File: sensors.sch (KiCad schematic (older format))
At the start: 0 parts

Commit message: Schematic: EEPROM + IMU
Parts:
- added C?: 10n, symbol C_Small
- added C? (x2): 100n, symbol C_Small
- added U?: MPU-9250, symbol MPU-9250
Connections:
- new net: C?.1, U?.10 (REGOUT)
- new net +3.3V_A: C?.1, C?.1, U?.13 (VDD), U?.19 (RESV), U?.8 (VDDIO)
- new net GND: C?.2, C?.2, C?.2, U?.18 (GND), U?.20 (RESV)
- new net SPI1_CS: U?.22 (nCS)
- new net SPI1_INT: U?.12 (INT)
- new net SPI1_MISO: U?.9 (AD0/SD0)
- new net SPI1_MOSI: U?.24 (SDA/SDI)
- new net SPI1_SCK: U?.23 (SCL/SCLK)
- no-connect marks 0 -> 13
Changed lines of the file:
@@
 LIBS:IRF
 LIBS:Comp2014
+LIBS:robocape-cache
 EELAYER 25 0
 EELAYER END
 $Descr A4 11693 8268
 encoding utf-8
-Sheet 1 3
+Sheet 2 4
 Title ""
 Date ""
@@
 Comment4 ""
 $EndDescr
+$Comp
+L MPU-9250 U?
+U 1 1 55A53A6C
+P 3750 2800
+F 0 "U?" H 4150 3600 60  0000 C CNN
+F 1 "MPU-9250" H 3500 3600 60  0000 C CNN
+F 2 "" H 3750 3400 60  0000 C CNN
+F 3 "" H 3750 3400 60  0000 C CNN
+	1    3750 2800
+	1    0    0    -1
+$EndComp
+NoConn ~ 2950 3500
+NoConn ~ 2950 3400
+NoConn ~ 2950 3300
+NoConn ~ 2950 3200
+NoConn ~ 2950 3100
+NoConn ~ 2950 3000
+NoConn ~ 2950 2900
+NoConn ~ 2950 2800
+NoConn ~ 2950 2700
+$Comp
+L +3.3V_A #PWR?
+U 1 1 55A53AEE
+P 2450 2125
+F 0 "#PWR?" H 2450 2085 30  0001 C CNN
+F 1 "+3.3V_A" H 2450 2235 30  0000 C CNN
+F 2 "" H 2450 2125 60  0000 C CNN
+F 3 "" H 2450 2125 60  0000 C CNN
+	1    2450 2125
+	1    0    0    -1
+$EndComp
+Wire Wire Line
+	2450 2150 2950 2150
+Wire Wire Line
+	2900 2150 2900 2250
+Wire Wire Line
+	2900 2250 2950 2250
+Connection ~ 2900 2150
+$Comp
+L GND #PWR?
+U 1 1 55A53B15
+P 2450 2475
+F 0 "#PWR?" H 2450 2225 50  0001 C CNN
+F 1 "GND" H 2450 2325 50  0000 C CNN
+F 2 "" H 2450 2475 60  0000 C CNN
+F 3 "" H 2450 2475 60  0000 C CNN
+	1    2450 2475
+	1    0    0    -1
+$EndComp
+Wire Wire Line
+	2450 2450 2950 2450
+$Comp
+L C_Small C?
+U 1 1 55A53B36
+P 2725 2300
+F 0 "C?" H 2735 2370 50  0000 L CNN
+F 1 "10n" H 2735 2220 50  0000 L CNN
+F 2 "" H 2725 2300 60  0000 C CNN
+F 3 "" H 2725 2300 60  0000 C CNN
+	1    2725 2300
+	1    0    0    -1
+$EndComp
+$Comp
+L C_Small C?
+U 1 1 55A53B7A
+P 2450 2300
+F 0 "C?" H 2460 2370 50  0000 L CNN
+F 1 "100n" H 2460 2220 50  0000 L CNN
+F 2 "" H 2450 2300 60  0000 C CNN
+F 3 "" H 2450 2300 60  0000 C CNN
+	1    2450 2300
+	1    0    0    -1
+$EndComp
+Wire Wire Line
+	2450 2125 2450 2200
+Connection ~ 2450 2150
+Wire Wire Line
+	2450 2400 2450 2475
+Connection ~ 2450 2450
+Wire Wire Line
+	2725 2400 2725 2450
+Connection ~ 2725 2450
+Wire Wire Line
+	2725 2200 2725 2150
+Connection ~ 2725 2150
+NoConn ~ 4550 2150
+NoConn ~ 4550 2250
+Text HLabel 4600 2400 2    39   Input ~ 0
+SPI1_SCK
+Wire Wire Line
+	4600 2400 4550 2400
+Text HLabel 4600 2500 2    39   Input ~ 0
+SPI1_MOSI
+Text HLabel 4600 2650 2    39   Input ~ 0
+SPI1_MISO
+Text HLabel 4600 2800 2    39   Input ~ 0
+SPI1_CS
+Wire Wire Line
+	4600 2500 4550 2500
+Wire Wire Line
+	4600 2650 4550 2650
+Wire Wire Line
+	4550 2800 4600 2800
+Text HLabel 4600 2950 2    39   Input ~ 0
+SPI1_INT
+Wire Wire Line
+	4600 2950 4550 2950
+$Comp
+L C_Small C?
+U 1 1 55A53E9E
+P 5025 3150
+F 0 "C?" H 5035 3220 50  0000 L CNN
+F 1 "100n" H 5035 3070 50  0000 L CNN
+F 2 "" H 5025 3150 60  0000 C CNN
+F 3 "" H 5025 3150 60  0000 C CNN
+	1    5025 3150
+	1    0    0    -1
+$EndComp
+NoConn ~ 4550 3150
+NoConn ~ 4550 3300
+$Comp
+L +3.3V_A #PWR?
+U 1 1 55A53F56
+P 4725 3400
+F 0 "#PWR?" H 4725 3360 30  0001 C CNN
+F 1 "+3.3V_A" H 4725 3510 30  0000 C CNN
+F 2 "" H 4725 3400 60  0000 C CNN
+F 3 "" H 4725 3400 60  0000 C CNN
+	1    4725 3400
+	1    0    0    -1
+$EndComp
+Wire Wire Line
+	4725 3400 4550 3400
+$Comp
+L GND #PWR?
+U 1 1 55A53F96
+P 4725 3500
+F 0 "#PWR?" H 4725 3250 50  0001 C CNN
+F 1 "GND" H 4725 3350 50  0000 C CNN
+F 2 "" H 4725 3500 60  0000 C CNN
+F 3 "" H 4725 3500 60  0000 C CNN
+	1    4725 3500
+	1    0    0    -1
+$EndComp
+Wire Wire Line
+	4725 3500 4550 3500
+$Comp
+L GND #PWR?
+U 1 1 55A53FE1
+P 5025 3300
+F 0 "#PWR?" H 5025 3050 50  0001 C CNN
+F 1 "GND" H 5025 3150 50  0000 C CNN
+F 2 "" H 5025 3300 60  0000 C CNN
+F 3 "" H 5025 3300 60  0000 C CNN
+	1    5025 3300
+	1    0    0    -1
+$EndComp
+Wire Wire Line
+	4550 3050 5025 3050
+Wire Wire Line
+	5025 3250 5025 3300
 $EndSCHEMATC

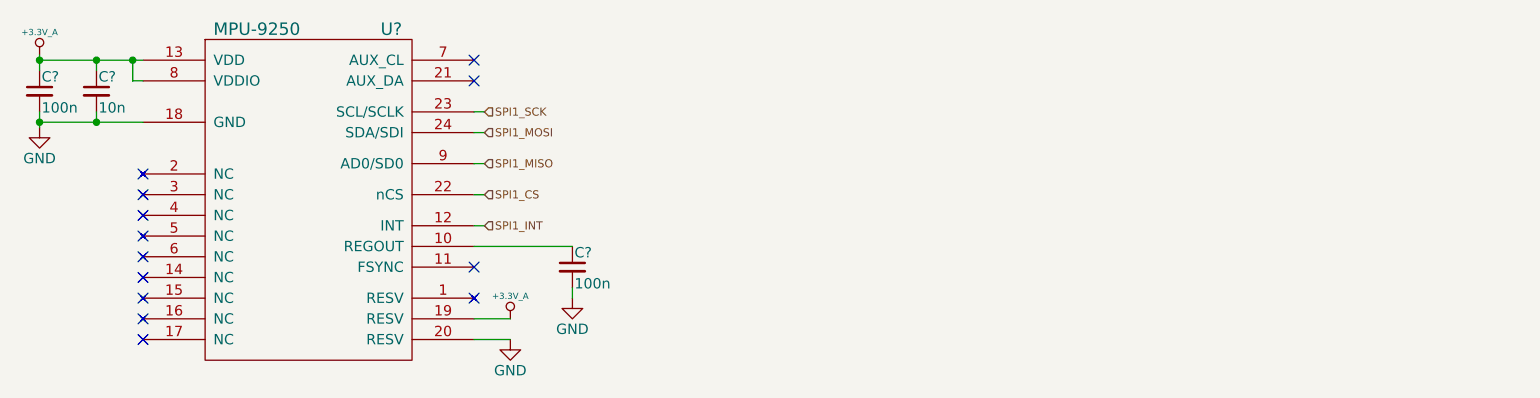
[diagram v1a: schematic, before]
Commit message: Schematic: Barometer
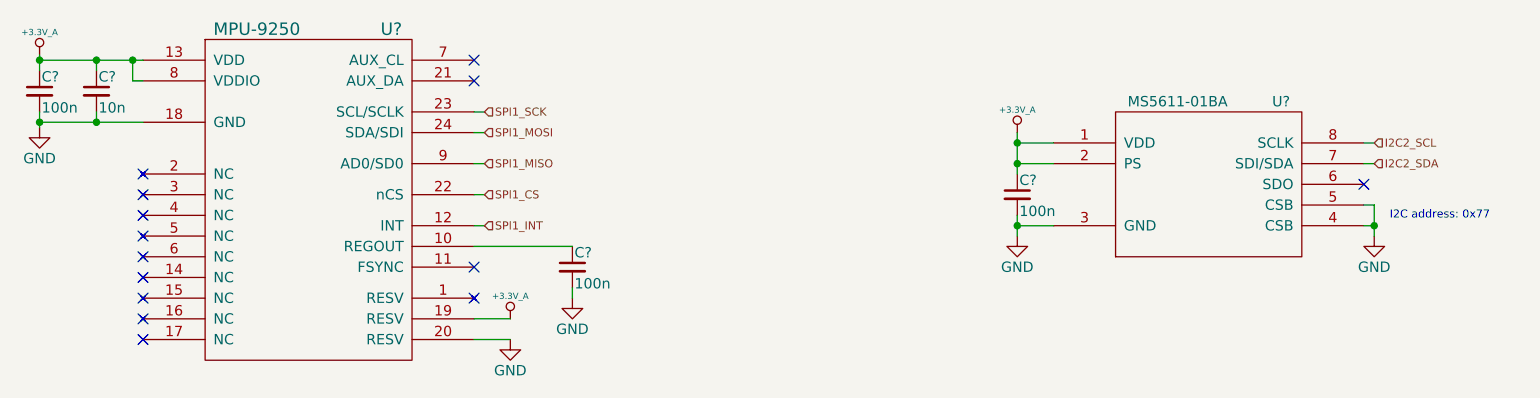
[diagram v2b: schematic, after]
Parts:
- added C?: 100n, symbol C_Small
- added U?: MS5611-01BA, MODULE, symbol MS5611-01BA
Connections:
- net +3.3V_A: now also C?.1, U?.1 (VDD), U?.2 (PS)
- net GND: now also C?.2, U?.3 (GND), U?.4 (CSB), U?.5 (CSB)
- new net I2C2_SCL: U?.8 (SCLK)
- new net I2C2_SDA: U?.7 (SDI/SDA)
- no-connect marks 13 -> 14
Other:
- note added: "I2C address: 0x77\n"
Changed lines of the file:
@@
 $Descr A4 11693 8268
 encoding utf-8
-Sheet 2 4
+Sheet 4 4
 Title ""
 Date ""
@@
 $EndComp
 Wire Wire Line
-	2450 2150 2950 2150
+	2450 2150 2725 2150
+Wire Wire Line
+	2725 2150 2900 2150
+Wire Wire Line
+	2900 2150 2950 2150
 Wire Wire Line
 	2900 2150 2900 2250
@@
 $EndComp
 Wire Wire Line
-	2450 2450 2950 2450
+	2450 2450 2725 2450
+Wire Wire Line
+	2725 2450 2950 2450
 $Comp
 L C_Small C?
@@
 $EndComp
 Wire Wire Line
-	2450 2125 2450 2200
+	2450 2125 2450 2150
+Wire Wire Line
+	2450 2150 2450 2200
 Connection ~ 2450 2150
 Wire Wire Line
-	2450 2400 2450 2475
+	2450 2400 2450 2450
+Wire Wire Line
+	2450 2450 2450 2475
 Connection ~ 2450 2450
 Wire Wire Line
@@
 Wire Wire Line
 	5025 3250 5025 3300
+$Comp
+L MS5611-01BA U?
+U 1 1 55A562A6
+P 8100 2750
+F 0 "U?" H 8450 3150 50  0000 C CNN
+F 1 "MS5611-01BA" H 7950 3150 50  0000 C CNN
+F 2 "MODULE" H 8100 2750 50  0001 C CNN
+F 3 "DOCUMENTATION" H 8100 2750 50  0001 C CNN
+	1    8100 2750
+	1    0    0    -1
+$EndComp
+NoConn ~ 8850 2750
+$Comp
+L GND #PWR?
+U 1 1 55A56310
+P 8900 3000
+F 0 "#PWR?" H 8900 2750 50  0001 C CNN
+F 1 "GND" H 8900 2850 50  0000 C CNN
+F 2 "" H 8900 3000 60  0000 C CNN
+F 3 "" H 8900 3000 60  0000 C CNN
+	1    8900 3000
+	1    0    0    -1
+$EndComp
+Wire Wire Line
+	8850 2850 8900 2850
+Wire Wire Line
+	8900 2850 8900 2950
+Wire Wire Line
+	8900 2950 8900 3000
+Wire Wire Line
+	8850 2950 8900 2950
+Connection ~ 8900 2950
+Text HLabel 8900 2650 2    39   Input ~ 0
+I2C2_SDA
+Text HLabel 8900 2550 2    39   Input ~ 0
+I2C2_SCL
+Wire Wire Line
+	8900 2550 8850 2550
+Wire Wire Line
+	8850 2650 8900 2650
+$Comp
+L +3.3V_A #PWR?
+U 1 1 55A56473
+P 7175 2500
+F 0 "#PWR?" H 7175 2460 30  0001 C CNN
+F 1 "+3.3V_A" H 7175 2610 30  0000 C CNN
+F 2 "" H 7175 2500 60  0000 C CNN
+F 3 "" H 7175 2500 60  0000 C CNN
+	1    7175 2500
+	1    0    0    -1
+$EndComp
+$Comp
+L C_Small C?
+U 1 1 55A564A3
+P 7175 2800
+F 0 "C?" H 7185 2870 50  0000 L CNN
+F 1 "100n" H 7185 2720 50  0000 L CNN
+F 2 "" H 7175 2800 60  0000 C CNN
+F 3 "" H 7175 2800 60  0000 C CNN
+	1    7175 2800
+	1    0    0    -1
+$EndComp
+Wire Wire Line
+	7350 2650 7175 2650
+Wire Wire Line
+	7175 2500 7175 2550
+Wire Wire Line
+	7175 2550 7175 2650
+Wire Wire Line
+	7175 2650 7175 2700
+Wire Wire Line
+	7175 2900 7175 2950
+Wire Wire Line
+	7175 2950 7175 3000
+Wire Wire Line
+	7175 2950 7350 2950
+Connection ~ 7175 2650
+Wire Wire Line
+	7350 2550 7175 2550
+Connection ~ 7175 2550
+$Comp
+L GND #PWR?
+U 1 1 55A566F0
+P 7175 3000
+F 0 "#PWR?" H 7175 2750 50  0001 C CNN
+F 1 "GND" H 7175 2850 50  0000 C CNN
+F 2 "" H 7175 3000 60  0000 C CNN
+F 3 "" H 7175 3000 60  0000 C CNN
+	1    7175 3000
+	1    0    0    -1
+$EndComp
+Connection ~ 7175 2950
+Text Notes 8975 2925 0    39   ~ 0
+I2C address: 0x77\n
 $EndSCHEMATC

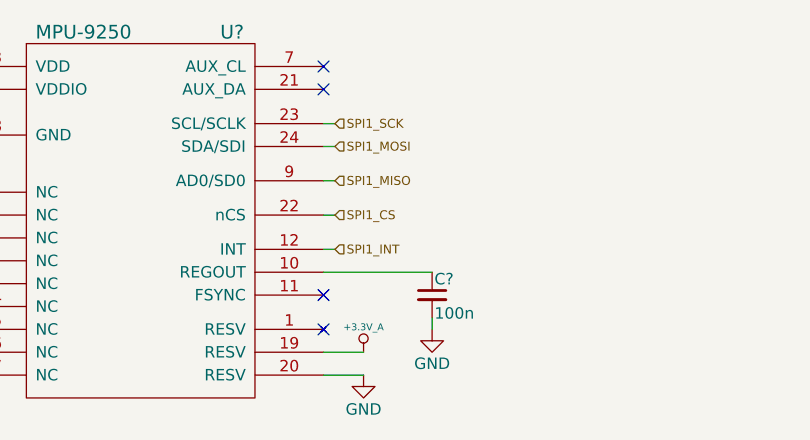
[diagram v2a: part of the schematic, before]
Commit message: Schematic: Xbee header
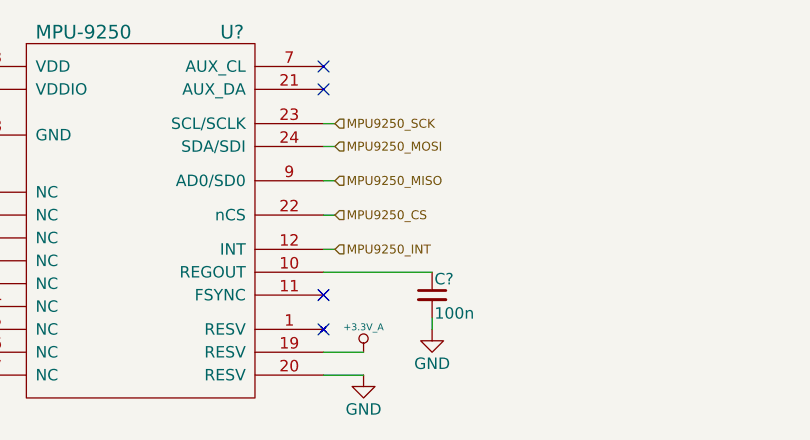
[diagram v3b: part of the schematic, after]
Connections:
- net SPI1_CS renamed MPU9250_CS
- net SPI1_INT renamed MPU9250_INT
- net SPI1_MISO renamed MPU9250_MISO
- net SPI1_MOSI renamed MPU9250_MOSI
- net SPI1_SCK renamed MPU9250_SCK
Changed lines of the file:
@@
 NoConn ~ 4550 2250
 Text HLabel 4600 2400 2    39   Input ~ 0
-SPI1_SCK
+MPU9250_SCK
 Wire Wire Line
 	4600 2400 4550 2400
 Text HLabel 4600 2500 2    39   Input ~ 0
-SPI1_MOSI
+MPU9250_MOSI
 Text HLabel 4600 2650 2    39   Input ~ 0
-SPI1_MISO
+MPU9250_MISO
 Text HLabel 4600 2800 2    39   Input ~ 0
-SPI1_CS
+MPU9250_CS
 Wire Wire Line
 	4600 2500 4550 2500
@@
 	4550 2800 4600 2800
 Text HLabel 4600 2950 2    39   Input ~ 0
-SPI1_INT
+MPU9250_INT
 Wire Wire Line
 	4600 2950 4550 2950

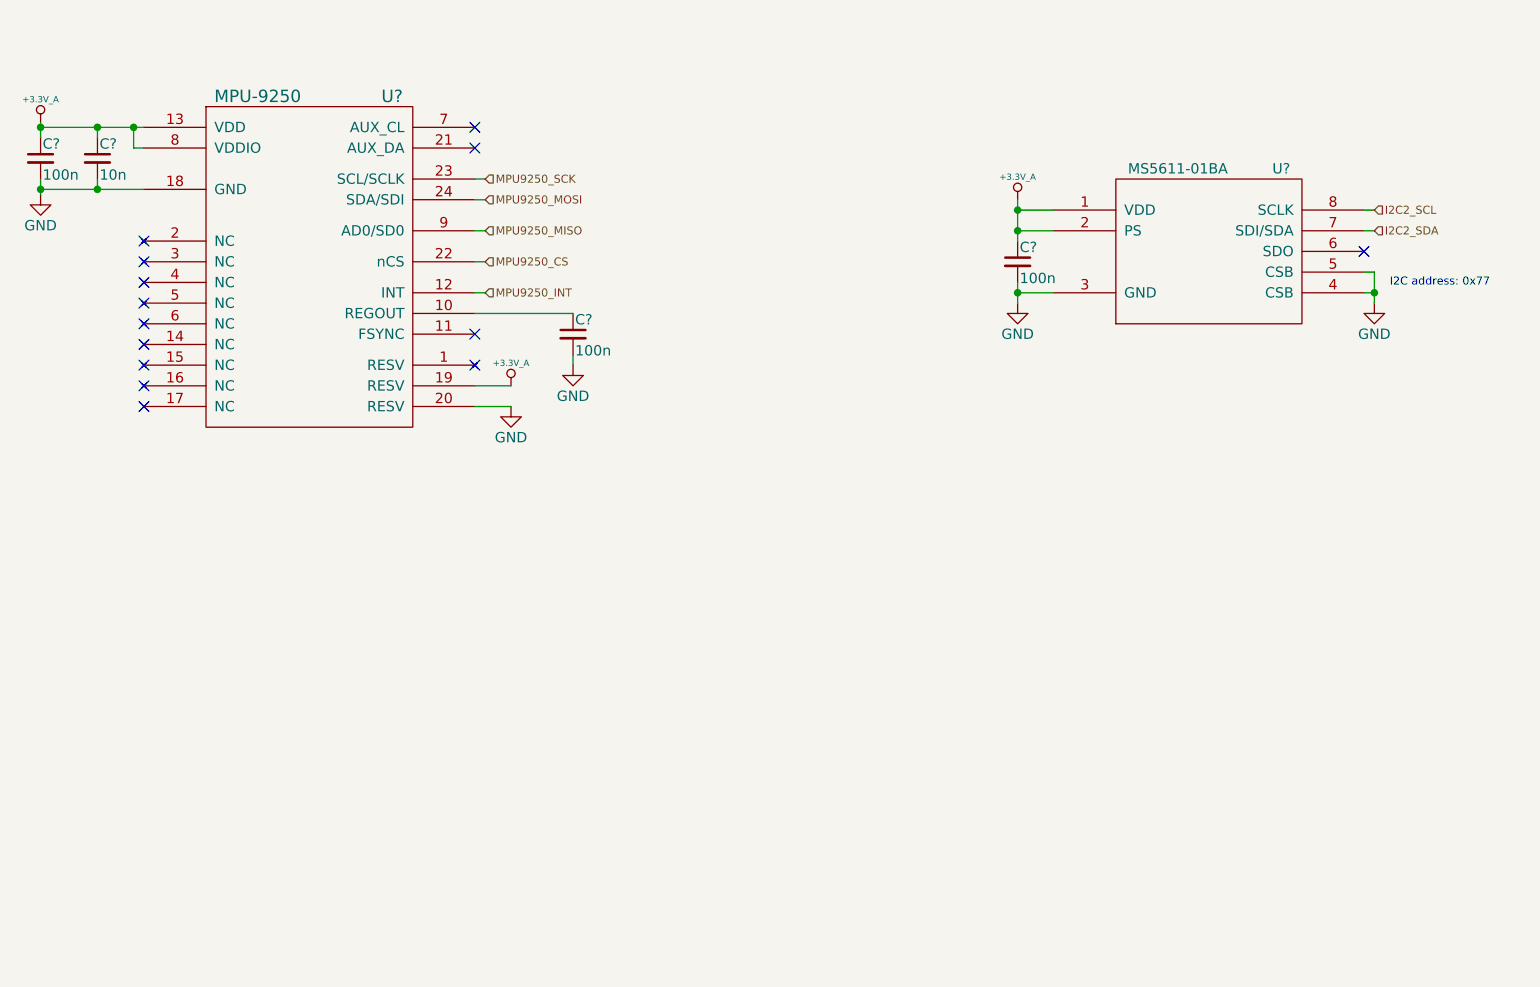
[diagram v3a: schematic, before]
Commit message: Schematics: GPS, Backup battery & Load Switch
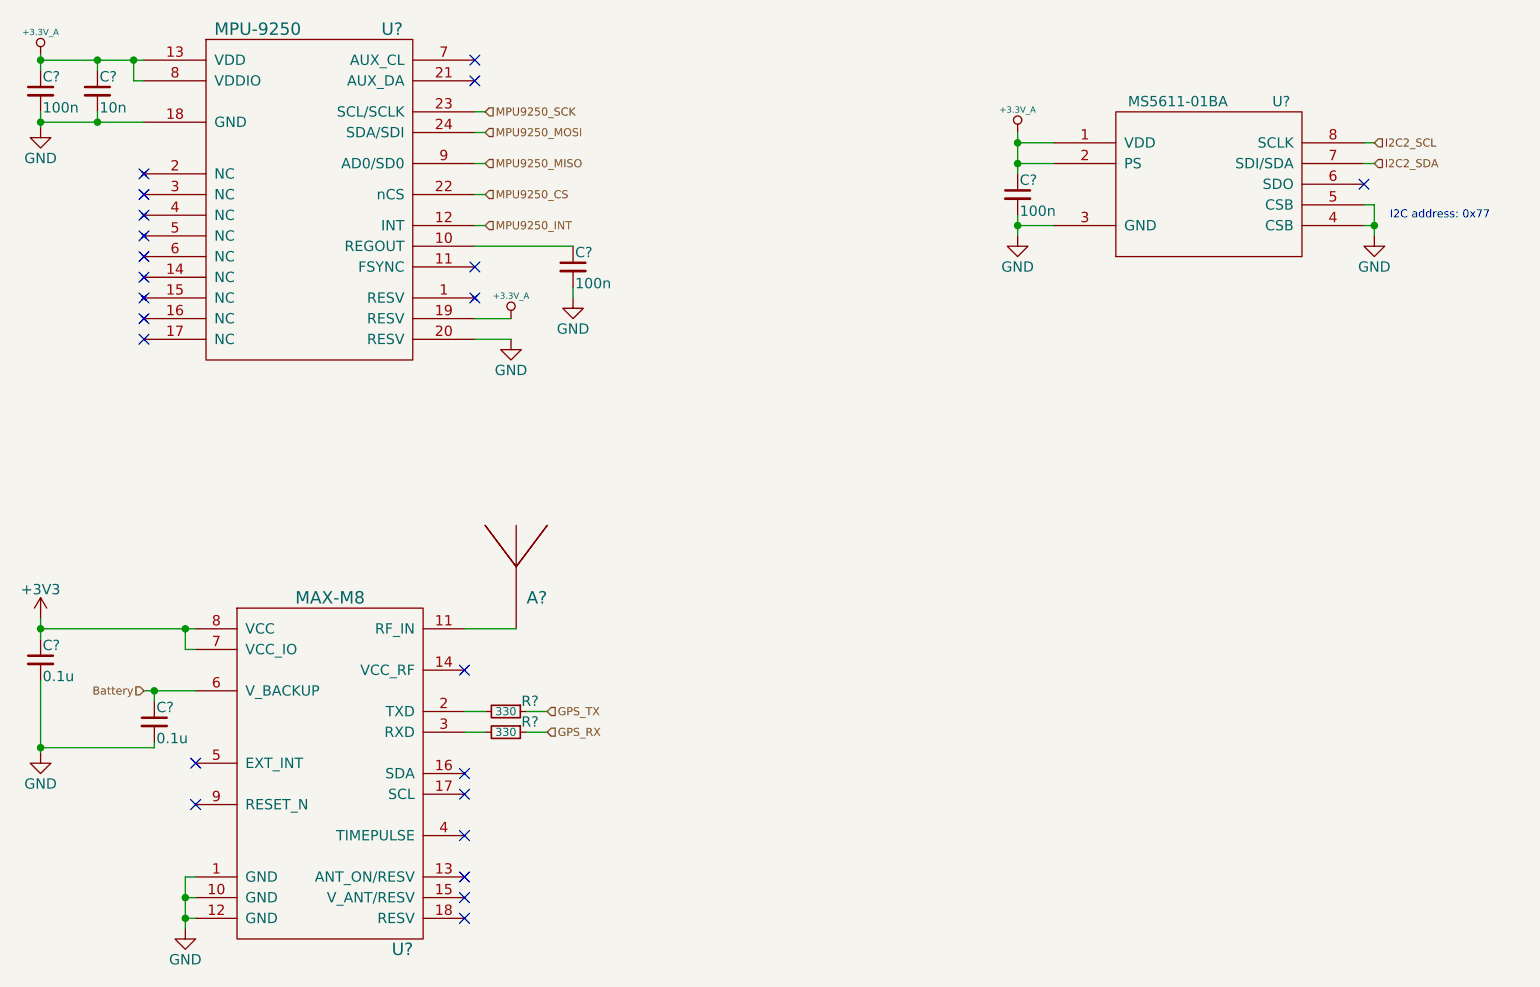
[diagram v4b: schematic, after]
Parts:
- added A?: ANTENNA, symbol ANTENNA
- added C? (x2): 0.1u, symbol C_Small
- added R? (x2): 330, symbol R_Small
- added U?: MAX-M8, symbol MAX-M8
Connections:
- net GND: now also C?.2, C?.2, U?.1 (GND), U?.10 (GND), U?.12 (GND)
- new net: A?.1 (ANTENNA), U?.11 (RF_IN)
- new net: R?.2, U?.2 (TXD)
- new net: R?.2, U?.3 (RXD)
- new net +3V3: C?.1, U?.7 (VCC_IO), U?.8 (VCC)
- new net Battery: C?.1, U?.6 (V_BACKUP)
- new net GPS_RX: R?.1
- new net GPS_TX: R?.1
- no-connect marks 14 -> 23
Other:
- moved on the sheet: C?, U?
